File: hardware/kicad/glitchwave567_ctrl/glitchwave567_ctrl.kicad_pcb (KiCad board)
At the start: 4 copper layers, 138 x 114 mm, 26 parts, among them J1 to MAIN 2x8 (B.Cu, mirrored), SW1 Suntsu SSWFS-S01 (TAP/BYP), SW2 Suntsu SSWFS-S01 (TAP/BYP)

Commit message: Fix CONTROL board stomp switches, regenerate fab release package
Replace the unsourceable Suntsu SSWFS-S01 stomp switch (SW1/SW2) with
Alpha SF12011F-0102-20R-M-011, verified against Alpha's SF12 series
datasheet (2.5mm pitch, Pin1=N.O./Pin2=COM/Pin3=N.C.). Updated the
footprint, schematic Value properties, and PCB routing (re-routed
around the new pad positions after the footprint swap moved absolute
pad locations onto pre-existing trace endpoints). CONTROL board DRC
and ERC are both clean (0 errors).

Also regenerates the full PCBWay fab release package:
- Gerbers for both MAIN and CONTROL boards (re-exported via KiCad)
- Turnkey BOM CSVs with MPNs for both boards (PCBWay format)
- Centroid/placement files for both boards
- BOM.xlsx updated with the new switch part
- README_PCBWAY.md updated to reflect the switch fix and DRC status
- All-in-one release zip with gerbers + BOM + centroid + KiCad source

Co-Authored-By: Claude Sonnet 5 <noreply@anthropic.com>
Claude-Session: https://claude.ai/code/session_012s26yHViqVd1t1x3TF8raS
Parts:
- SW1: value Suntsu SSWFS-S01 (TAP/BYP) -> Alpha SF12011F-0102-20R-M-011 (TAP/BYP); footprint SSWFS-S01 -> SF12011F-0102-M
- SW2: value Suntsu SSWFS-S01 (TAP/BYP) -> Alpha SF12011F-0102-20R-M-011 (TAP/TEMPO); footprint SSWFS-S01 -> SF12011F-0102-M
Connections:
- SW1 pad 1: /STOMP1 -> GND
- SW1 pad 2: GND -> /STOMP1
- SW2 pad 1: /STOMP2 -> GND
- SW2 pad 2: GND -> /STOMP2
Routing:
- net /POT6_W: track 44.9 -> 54.8 mm
- net /STOMP1: track 83.8 -> 92.6 mm
- net /STOMP2: track 10.1 -> 15.5 mm

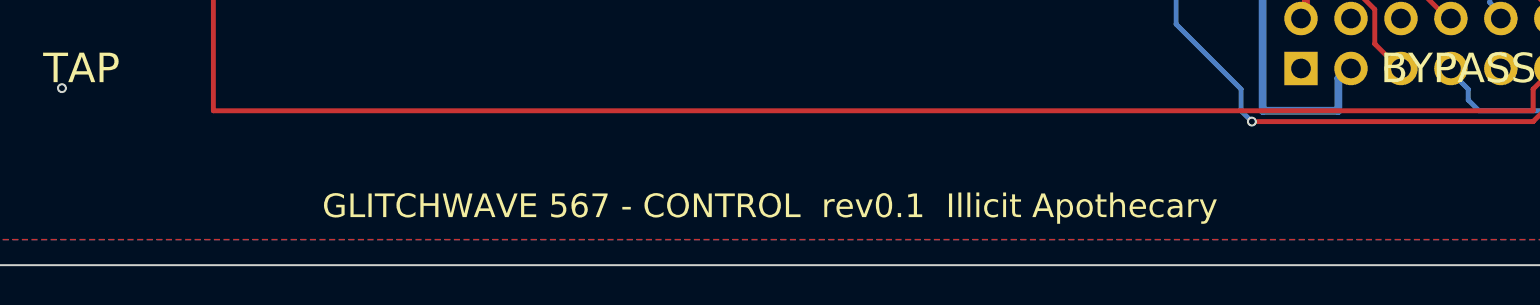
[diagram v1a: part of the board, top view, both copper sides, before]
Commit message: hardware: fix C107 duplicate refdes, add missing courtyards, rename silkscreen
Pre-order verification pass before sending the boards to PCBWay. Full write-up in
hardware/fab/ORDER_READINESS_20260911.md.

C107 was a duplicate reference designator: a 100n 0603 on FREQ_CV in mcu.kicad_sch
and a 22uF 0805 in power.kicad_sch that is the MP1584's second output capacitor.
Only the 100n existed on the PCB, so the +5V rail (Pico plus six WS2812B via J10)
would have been built with half its intended bulk capacitance, and the BOM listed
C107 twice with conflicting parts. KiCad collapses a duplicate refdes to one
component, so footprint count matched symbol count, DRC schematic parity passed and
ERC said nothing. Only a designator-level BOM-vs-board-vs-CPL diff finds it.

  - power.kicad_sch: the 22uF symbol renamed C107 to C112
  - MAIN PCB: C112 placed at (62.6, 25.0), 0.3mm F.Cu stub to the +5V trunk at
    y=23.65, GND through the F.Cu pour exactly as C108 is connected. Placement
    chosen by a clearance search, nearest obstacle 0.42mm against a 0.13mm rule.
    No via: every via position in that pocket scored under 0.23mm against the
    In2.Cu diagonals. Zones refilled.
  - BOM.xlsx: the 22uF row's designators changed from C107,C108 to C108,C112

Courtyards added to the 13 footprints that had none (J1-J6 and U20 on MAIN,
RV1-RV6 on CONTROL), copied from the library footprints. DRC was structurally blind
to body collisions on exactly the largest mechanical parts, which is why both jack
collisions went undetected in July. Every footprint on both boards now has one.
That exposed two more courtyard overlaps on MAIN, both courtyard-only with the
bodies clear: J5 to FB100 (0.700mm of body air, ~0.21mm of copper) and J4 to R98
(0.338mm). Nothing was moved because nothing collides.

Silkscreen on both boards renamed from "GLITCHWAVE 567" to "WHERE THE FUZZ MEETS
THE FUNK". Font 1.2 to 1.0mm so the longer string keeps about the same width:
measured in the plotted gerber it spans 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
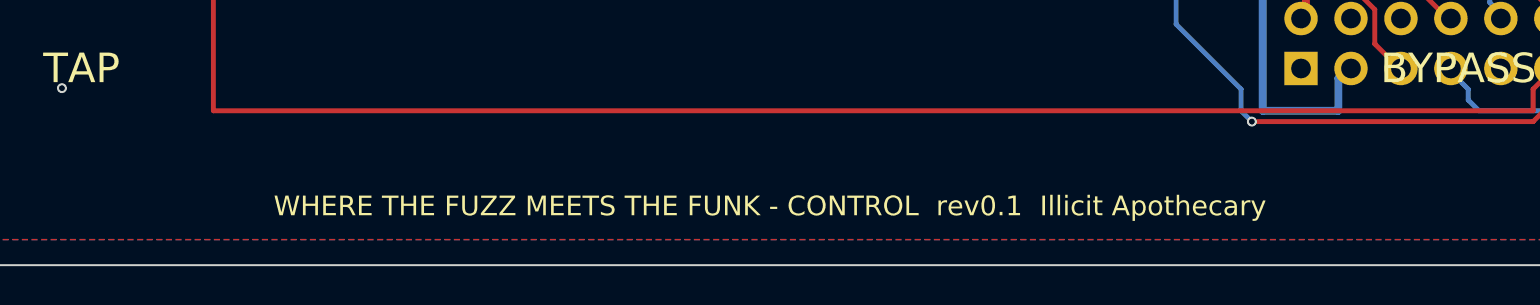
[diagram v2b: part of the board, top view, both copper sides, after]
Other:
- board text added: "WHERE THE FUZZ MEETS THE FUNK - CONTROL rev0.1 Illicit Apothecary"
- board text removed: "GLITCHWAVE 567 - CONTROL rev0.1 Illicit Apothecary"
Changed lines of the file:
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@@
 			)
 		)
+		(fp_line
+			(start -6.1 -5.75)
+			(end 6.1 -5.75)
+			(stroke
+				(width 0.05)
+				(type solid)
+			)
+			(layer "F.CrtYd")
+		)
+		(fp_line
+			(start 6.1 -5.75)
+			(end 6.1 8.15)
+			(stroke
+				(width 0.05)
+				(type solid)
+			)
+			(layer "F.CrtYd")
+		)
+		(fp_line
+			(start 6.1 8.15)
+			(end -6.1 8.15)
+			(stroke
+				(width 0.05)
+				(type solid)
+			)
+			(layer "F.CrtYd")
+		)
+		(fp_line
+			(start -6.1 8.15)
+			(end -6.1 -5.75)
+			(stroke
+				(width 0.05)
+				(type solid)
+			)
+			(layer "F.CrtYd")
+		)
 		(pad "1" thru_hole circle
 			(at -2.5 7)
@@
 			)
 		)
+		(fp_line
+			(start -6.1 -5.75)
+			(end 6.1 -5.75)
+			(stroke
+				(width 0.05)
+				(type solid)
+			)
+			(layer "F.CrtYd")
+		)
+		(fp_line
+			(start 6.1 -5.75)
+			(end 6.1 8.15)
+			(stroke
+				(width 0.05)
+				(type solid)
+			)
+			(layer "F.CrtYd")
+		)
+		(fp_line
+			(start 6.1 8.15)
+			(end -6.1 8.15)
+			(stroke
+				(width 0.05)
+				(type solid)
+			)
+			(layer "F.CrtYd")
+		)
+		(fp_line
+			(start -6.1 8.15)
+			(end -6.1 -5.75)
+			(stroke
+				(width 0.05)
+				(type solid)
+			)
+			(layer "F.CrtYd")
+		)
 		(pad "1" thru_hole circle
 			(at -2.5 7)
@@
 			)
 		)
+		(fp_line
+			(start -6.1 -5.75)
+			(end 6.1 -5.75)
+			(stroke
+				(width 0.05)
+				(type solid)
+			)
+			(layer "F.CrtYd")
+		)
+		(fp_line
+			(start 6.1 -5.75)
+			(end 6.1 8.15)
+			(stroke
+				(width 0.05)
+				(type solid)
+			)
+			(layer "F.CrtYd")
+		)
+		(fp_line
+			(start 6.1 8.15)
+			(end -6.1 8.15)
+			(stroke
+				(width 0.05)
+				(type solid)
+			)
+			(layer "F.CrtYd")
+		)
+		(fp_line
+			(start -6.1 8.15)
+			(end -6.1 -5.75)
+			(stroke
+				(width 0.05)
+				(type solid)
+			)
+			(layer "F.CrtYd")
+		)
 		(pad "1" thru_hole circle
 			(at -2.5 7)
@@
 			)
 		)
+		(fp_line
+			(start -6.1 -5.75)
+			(end 6.1 -5.75)
+			(stroke
+				(width 0.05)
+				(type solid)
+			)
+			(layer "F.CrtYd")
+		)
+		(fp_line
+			(start 6.1 -5.75)
+			(end 6.1 8.15)
+			(stroke
+				(width 0.05)
+				(type solid)
+			)
+			(layer "F.CrtYd")
+		)
+		(fp_line
+			(start 6.1 8.15)
+			(end -6.1 8.15)
+			(stroke
+				(width 0.05)
+				(type solid)
+			)
+			(layer "F.CrtYd")
+		)
+		(fp_line
+			(start -6.1 8.15)
+			(end -6.1 -5.75)
+			(stroke
+				(width 0.05)
+				(type solid)
+			)
+			(layer "F.CrtYd")
+		)
 		(pad "1" thru_hole circle
 			(at -2.5 7)
@@
 			)
 		)
+		(fp_line
+			(start -6.1 -5.75)
+			(end 6.1 -5.75)
+			(stroke
+				(width 0.05)
+				(type solid)
+			)
+			(layer "F.CrtYd")
+		)
+		(fp_line
+			(start 6.1 -5.75)
+			(end 6.1 8.15)
+			(stroke
+				(width 0.05)
+				(type solid)
+			)
+			(layer "F.CrtYd")
+		)
+		(fp_line
+			(start 6.1 8.15)
+			(end -6.1 8.15)
+			(stroke
+				(width 0.05)
+				(type solid)
+			)
+			(layer "F.CrtYd")
+		)
+		(fp_line
+			(start -6.1 8.15)
+			(end -6.1 -5.75)
+			(stroke
+				(width 0.05)
+				(type solid)
+			)
+			(layer "F.CrtYd")
+		)
 		(pad "1" thru_hole circle
 			(at -2.5 7)
@@
 			)
 		)
+		(fp_line
+			(start -6.1 -5.75)
+			(end 6.1 -5.75)
+			(stroke
+				(width 0.05)
+				(type solid)
+			)
+			(layer "F.CrtYd")
+		)
+		(fp_line
+			(start 6.1 -5.75)
+			(end 6.1 8.15)
+			(stroke
+				(width 0.05)
+				(type solid)
+			)
+			(layer "F.CrtYd")
+		)
+		(fp_line
+			(start 6.1 8.15)
+			(end -6.1 8.15)
+			(stroke
+				(width 0.05)
+				(type solid)
+			)
+			(layer "F.CrtYd")
+		)
+		(fp_line
+			(start -6.1 8.15)
+			(end -6.1 -5.75)
+			(stroke
+				(width 0.05)
+				(type solid)
+			)
+			(layer "F.CrtYd")
+		)
 		(pad "1" thru_hole circle
 			(at -2.5 7)
@@
 		(layer "Edge.Cuts")
 	)
-	(gr_text "GLITCHWAVE 567 - CONTROL  rev0.1  Illicit Apothecary"
+	(gr_text "WHERE THE FUZZ MEETS THE FUNK - CONTROL  rev0.1  Illicit Apothecary"
 		(at 69 111 0)
 		(layer "F.SilkS")
 		(effects
 			(font
-				(size 1.2 1.2)
+				(size 1 1)
 			)
 		)

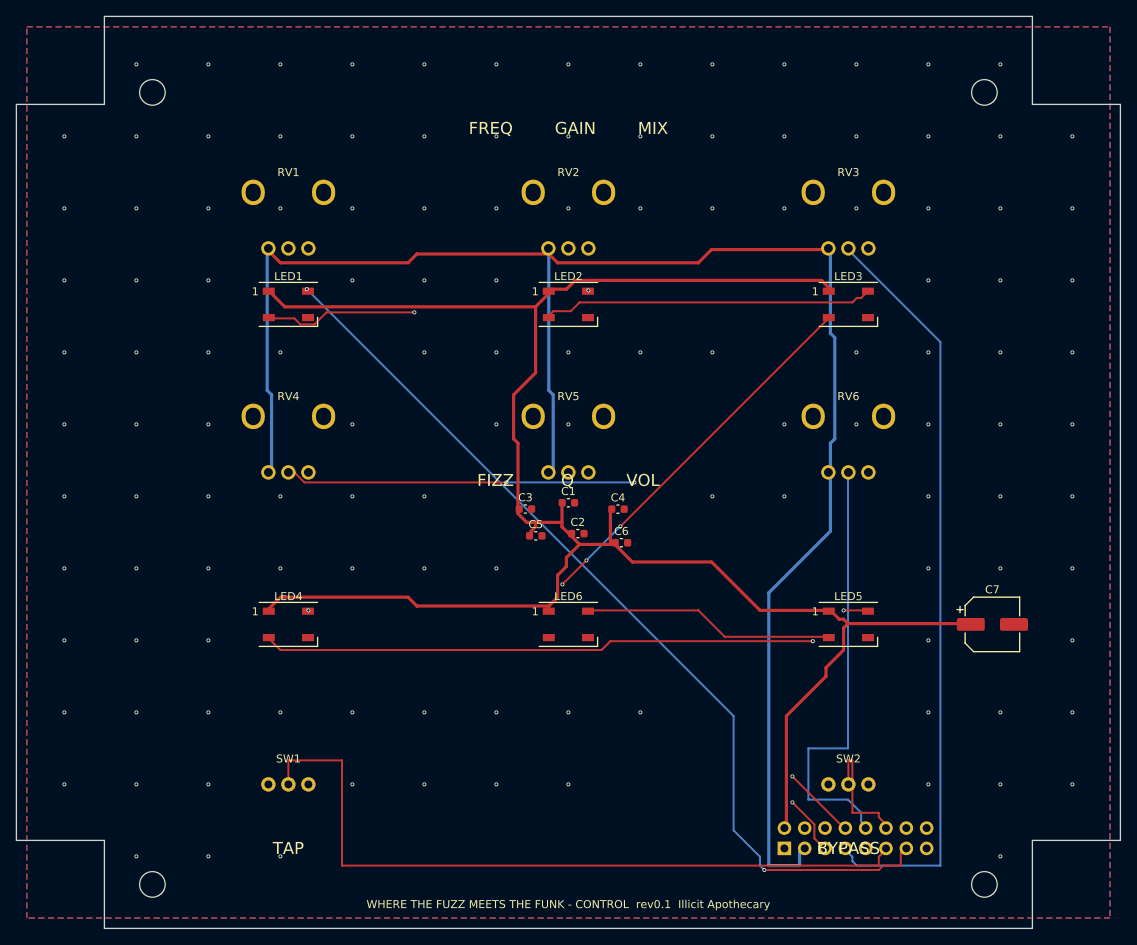
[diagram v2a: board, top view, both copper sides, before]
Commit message: Rev 8: third stomp (SW3) + STOMP3 to GP22, boards/BOM/fab package updated
CONTROL: SW3 at (69,96); SW1/SW2 outboard to 23.28/114.72 (1.800in pitch);
LED4/LED5 follow; C7 +1.5mm east; 3 GND stitch vias cleared from new pad rows;
/POT3_W detoured around SW2's new COM pad; stomp silk now A/B/C; STOMP3 on
spare J1 pin 15. Fixes schematic pin1/pin3 inversion on SW1/SW2 (GND belongs
on N.O.; PCB was already right). DRC 0 errors.

MAIN: R175 10k pullup + C125 100n added; STOMP3 routed J10.15 -> GP22 (Pico
pad 29). DRC/ERC at pre-existing baselines. BOM.xlsx updated (SW qty 3, R/C
qty bumps, stale Suntsu README lines replaced). Fab package regenerated both
boards: Glitchwave567_PCBWay_Release_20260921.zip, README_PCBWAY rev 0.6.

Enclosure drill template still stale: needs three D12.2 at centreline +/-45.72mm.

Co-Authored-By: Claude Fable 5 <noreply@anthropic.com>
Claude-Session: https://claude.ai/code/session_01ArRoxLtCyE7DZoHE3DcYLs
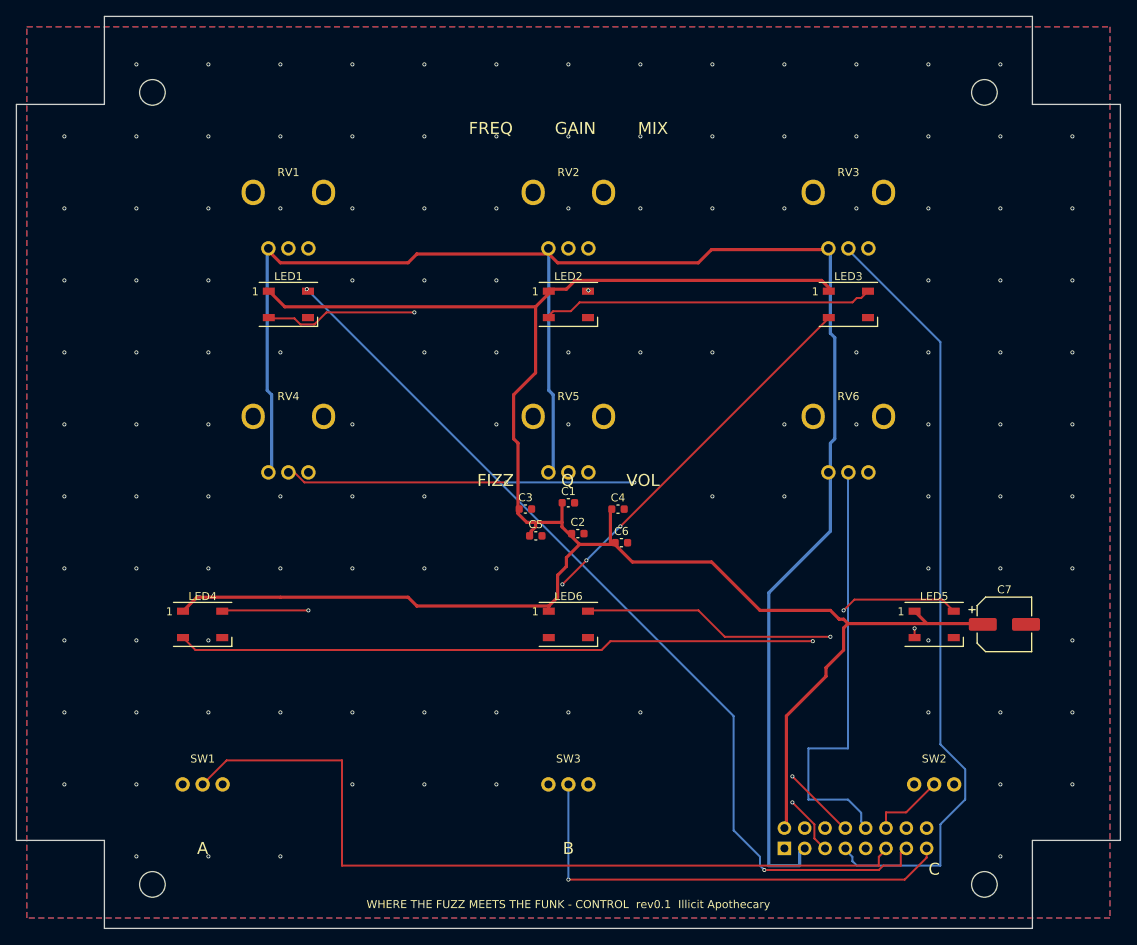
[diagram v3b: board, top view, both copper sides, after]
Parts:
- added SW3: Alpha SF12011F-0102-20R-M-011 (STOMP3), SF12011F-0102-M, F.Cu at (69.0, 96.0)
- moved LED4 10.7 mm to (23.3, 76.0)
- moved LED5 10.7 mm to (114.7, 76.0)
- moved SW1 10.7 mm to (23.3, 96.0)
- moved SW2 10.7 mm to (114.7, 96.0)
- moved C7 1.50 mm to (123.5, 76.0)
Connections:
- J1 pad 15: unconnected-(J1-Pin_15-Pad15) -> /STOMP3
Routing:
- net /STOMP3: track 0.00 -> 59.0 mm, vias 0 -> 1
- net /WSD4: track 78.1 -> 100.2 mm
- net +5V: track 246.5 -> 259.2 mm
- net /WSD5: track 31.6 -> 43.7 mm, vias 0 -> 2
- net /WSD3: track 80.3 -> 91.1 mm
- net /STOMP1: track 92.6 -> 101.6 mm
- net /STOMP2: track 15.5 -> 9.43 mm
- net /POT3_W: track 95.1 -> 97.7 mm
- net GND: vias 128 -> 125
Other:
- board text added: "A"
- board text added: "B"
- board text added: "C"
- board text removed: "BYPASS"
- board text removed: "TAP"
